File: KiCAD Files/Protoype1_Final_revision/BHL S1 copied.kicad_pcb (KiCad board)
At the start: 4 copper layers, 64 x 64 mm, 104 parts, among them IC1 NUP2105LT1G, IC2 NUP2105LT1G, IC4 FD6288Q, J1 39-30-1042, J2 Conn_01x03_Pin, J3 Conn_01x03_Pin, J4 39-30-1042, Q1 CSD19502Q5B, Q2 CSD19502Q5B, Q3 CSD19502Q5B, Q4 CSD19502Q5B, Q5 CSD19502Q5B, Q7 CSD19502Q5B, U1 ME6211C30M5, U2 SPX3819M5-L-5-0, U3 Solder Pad, U5 STM32G431CBU6, Y1 8MHz

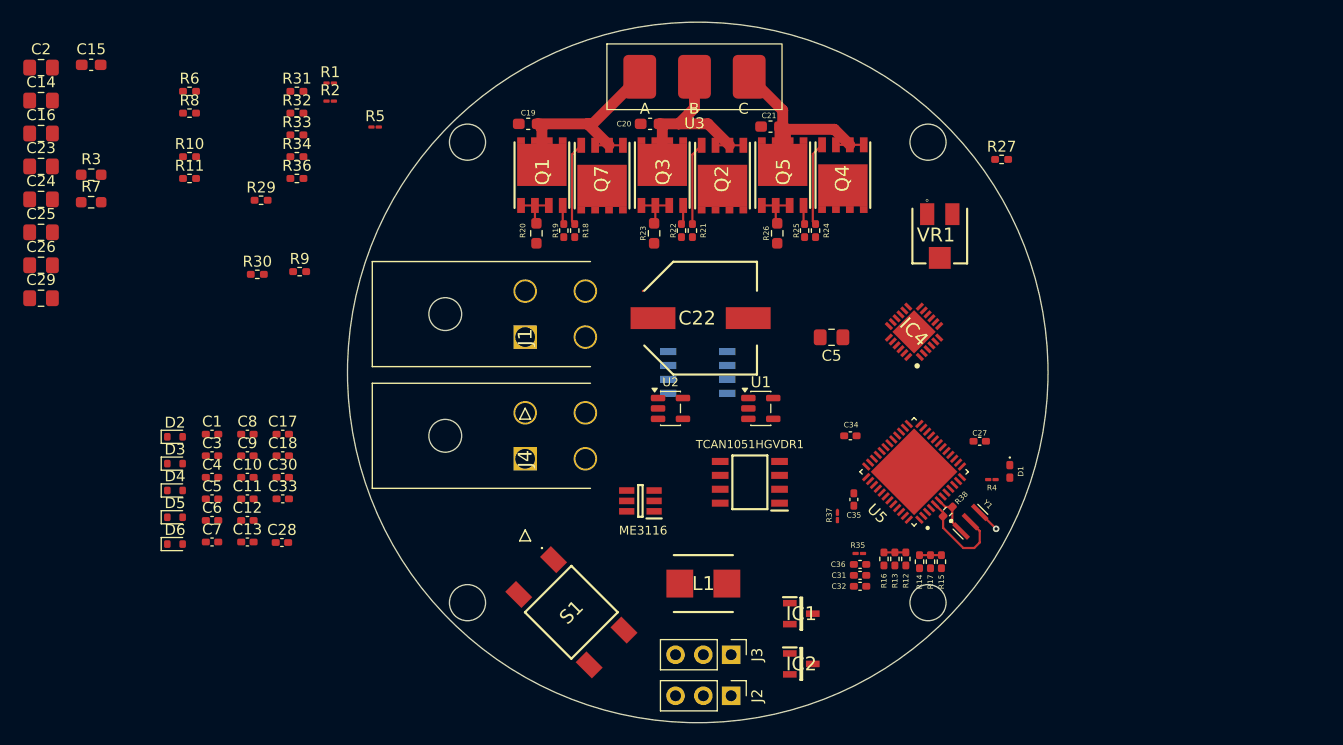
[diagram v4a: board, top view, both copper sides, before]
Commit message: Routed half the gate driver
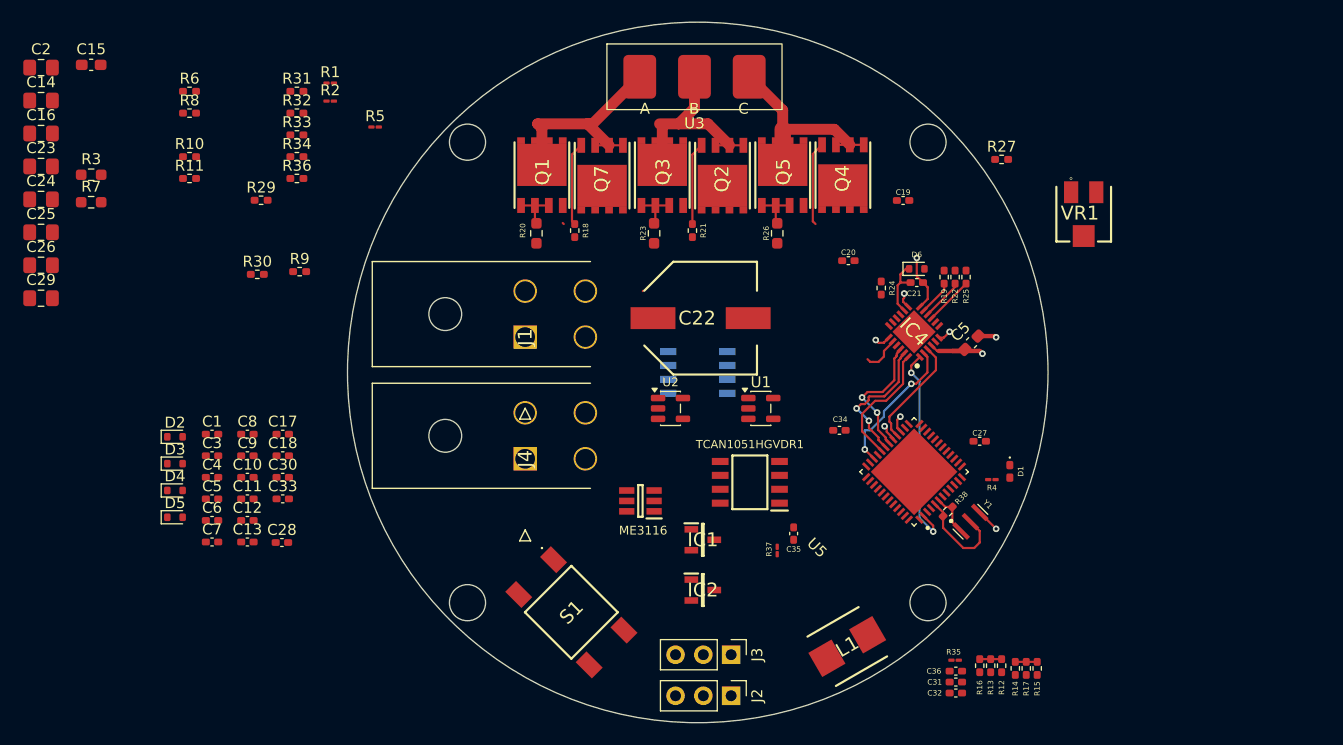
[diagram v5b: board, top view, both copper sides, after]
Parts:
- C19, C20, C21: footprint Capacitor_SMD:C_0603_1608Metric_Pad1.08x0.95mm_HandSolder -> Capacitor_SMD:C_0402_1005Metric_Pad0.74x0.62mm_HandSolder
- C5: footprint Capacitor_SMD:C_0805_2012Metric_Pad1.18x1.45mm_HandSolder -> Capacitor_SMD:C_0603_1608Metric_Pad1.08x0.95mm_HandSolder
- moved D6 72.3 mm to (217.8, 74.0)
- moved R19 35.0 mm to (220.2, 74.8)
- moved C19 35.0 mm to (216.5, 67.8)
- moved R22 25.4 mm to (221.2, 74.8)
- moved C20 22.0 mm to (211.5, 73.2)
- moved C21 19.5 mm to (217.8, 75.2)
- moved R25 15.4 mm to (222.2, 74.8)
- moved L1 14.4 mm to (211.4, 108.5), turned to 30 degrees
- moved VR1 13.3 mm to (233.0, 69.0)
- moved C31 13.1 mm to (221.3, 111.8)
- moved C32 13.1 mm to (221.3, 112.8)
- moved C36 13.1 mm to (221.3, 110.8)
- moved R12 13.1 mm to (225.5, 110.2)
- moved R13 13.1 mm to (223.5, 110.2)
- moved R14 13.1 mm to (226.8, 110.5)
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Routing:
- net LIN1: track 0.00 -> 18.9 mm, vias 0 -> 2
- net LIN2: track 0.00 -> 13.1 mm, vias 0 -> 2
- net HIN2: track 0.00 -> 12.5 mm, vias 0 -> 2
- net HIN1: track 0.00 -> 11.9 mm, vias 0 -> 2
- net HIN3: track 0.00 -> 11.7 mm
- net LIN3: track 0.00 -> 10.3 mm
- net VCC_12V: track 0.00 -> 6.17 mm, vias 0 -> 1
- net VB3: track 0.00 -> 5.60 mm
- net SH_C: track 18.9 -> 24.1 mm, vias 0 -> 1
- net GL_C: track 0.00 -> 4.48 mm
- net GL_B: track 0.00 -> 3.85 mm
- net VB1: track 0.00 -> 3.51 mm
- net GL_A: track 0.00 -> 3.23 mm
- net GND: track 1.77 -> 4.62 mm, vias 1 -> 3
- net Net-(Q3-G): track 1.76 -> 0.00 mm
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
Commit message: Finished Routing the Gate Driver!
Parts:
- R20, R23, R26: footprint Resistor_SMD:R_0603_1608Metric_Pad0.98x0.95mm_HandSolder -> Resistor_SMD:R_1206_3216Metric_Pad1.30x1.75mm_HandSolder
- moved D5 66.6 mm to (213.2, 75.8), turned to 45 degrees
- moved D4 62.4 mm to (210.8, 80.0), turned to 90 degrees
- moved C31 25.4 mm to (246.7, 112.0)
- moved C32 25.4 mm to (246.7, 113.0)
- moved C36 25.4 mm to (246.7, 111.0)
- moved R12 25.4 mm to (250.9, 110.5)
- moved R13 25.4 mm to (248.9, 110.5)
- moved R14 25.4 mm to (252.1, 110.8)
- moved R15 25.4 mm to (254.1, 110.8)
- moved R16 25.4 mm to (249.9, 110.5)
- moved R17 25.4 mm to (253.1, 110.8)
- moved R35 25.4 mm to (246.6, 110.0)
- moved C19 12.8 mm to (212.8, 80.0), turned to 90 degrees
- moved R24 10.4 mm to (204.5, 72.8), turned to 0 degrees
- moved R18 6.77 mm to (179.8, 70.0)
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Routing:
- net GH_A: track 1.51 -> 41.0 mm, vias 1 -> 2
- net Net-(Q1-G): track 0.13 -> 37.3 mm, vias 0 -> 2
- net Net-(Q3-G): track 0.00 -> 27.4 mm, vias 0 -> 2
- net GH_B: track 0.00 -> 24.5 mm, vias 0 -> 2
- net SH_A: track 20.3 -> 40.2 mm, vias 0 -> 2
- net Net-(Q5-G): track 0.00 -> 13.8 mm
- net GH_C: track 1.45 -> 15.2 mm, vias 1 -> 2
- net SH_B: track 18.1 -> 29.4 mm, vias 0 -> 2
- net VB2: track 0.00 -> 5.22 mm
- net SH_C: track 24.1 -> 19.1 mm, vias 1 -> 2
- net VCC_12V: track 6.17 -> 10.6 mm, vias 1 -> 4
- net Vshunt_1+: track 4.33 -> 0.00 mm
- net Vshunt_3+: track 4.23 -> 0.00 mm
- net Vshunt_2+: track 4.22 -> 0.00 mm
- net Net-(Q2-G): track 7.54 -> 11.5 mm
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- added copper zone on In2.Cu, net DCBUS
- added copper zone on F.Cu, net GND
- added copper zone on F.Cu, net SH_A
- added copper zone on F.Cu, net SH_B
- added copper zone on F.Cu, net SH_C
- added copper zone on F.Cu, net Vshunt_1+
- added copper zone on F.Cu, net Vshunt_2+
- added copper zone on F.Cu, net Vshunt_3+

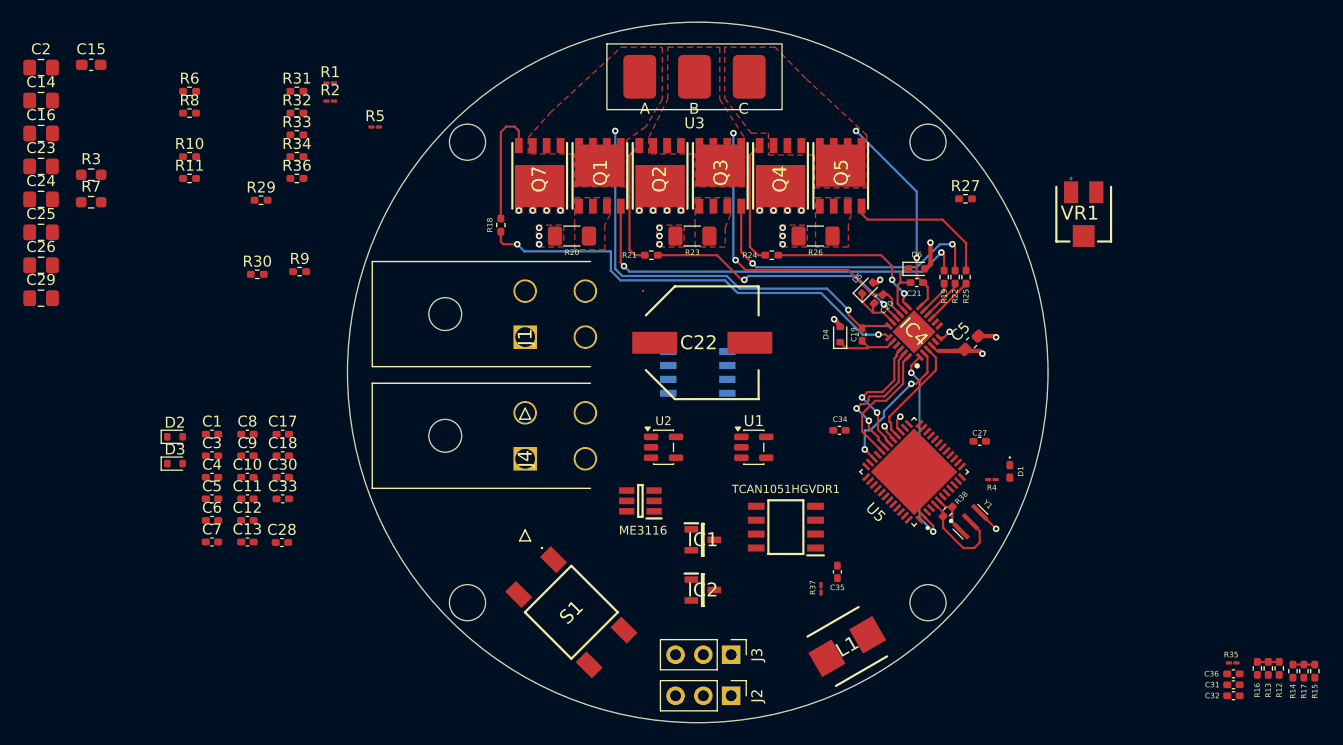
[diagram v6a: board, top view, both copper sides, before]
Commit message: Can Bus Routed In PCB
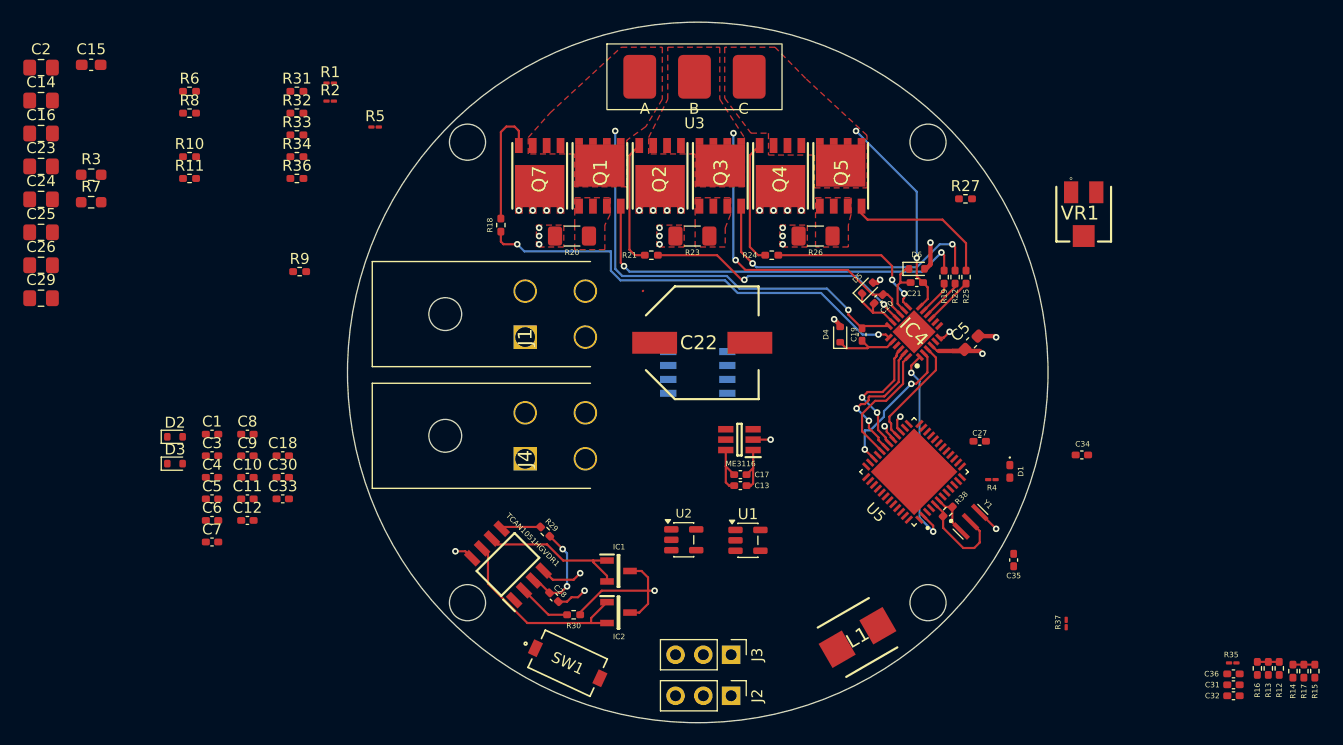
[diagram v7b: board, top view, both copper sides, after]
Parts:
- removed S1: 1571563-6, Footprint for BHL S1:Push Button 6x6mm
- added SW1: PTS636 SM50J SMTR LFS, Footprint for BHL S1:SW_PTS636_CNK, F.Cu at (185.9, 110.0)
- moved C13 45.3 mm to (201.6, 93.8), turned to 180 degrees
- moved R30 42.5 mm to (186.4, 105.6)
- moved C17 42.0 mm to (201.6, 92.8), turned to 180 degrees
- moved R29 39.9 mm to (183.8, 98.0), turned to 135 degrees
- moved TCAN1051HGVDR1 25.6 mm to (180.4, 101.0), turned to 135 degrees
- moved C28 25.3 mm to (184.6, 104.0), turned to -45 degrees
- moved R37 22.6 mm to (231.4, 106.4)
- moved C34 22.3 mm to (232.8, 91.0)
- moved C35 16.1 mm to (226.6, 100.6)
- moved ME3116 10.6 mm to (201.6, 89.6)
- moved U2 8.65 mm to (196.5, 98.8)
- moved U1 8.52 mm to (202.3, 98.8)
- moved IC1 8.21 mm to (190.5, 101.6)
- moved IC2 7.97 mm to (190.5, 105.4)
- moved L1 1.25 mm to (212.3, 107.7)
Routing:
- net GND: track 4.62 -> 29.8 mm, vias 12 -> 16
- net CAN_H: track 0.00 -> 18.3 mm
- net CAN_L: track 0.00 -> 14.0 mm
- net VCC_5V: track 0.00 -> 8.98 mm, vias 0 -> 2
- net Net-(D2-K): track 0.00 -> 4.92 mm
- net Net-(ME3116-BS): track 0.00 -> 4.58 mm
- net CAN_RX: track 0.00 -> 3.93 mm, vias 0 -> 1
- net Net-(TCAN1051HGVDR1-VIO): track 0.00 -> 3.61 mm

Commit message: Finished Buck Converter, Switch, and Temp Resistor Routing
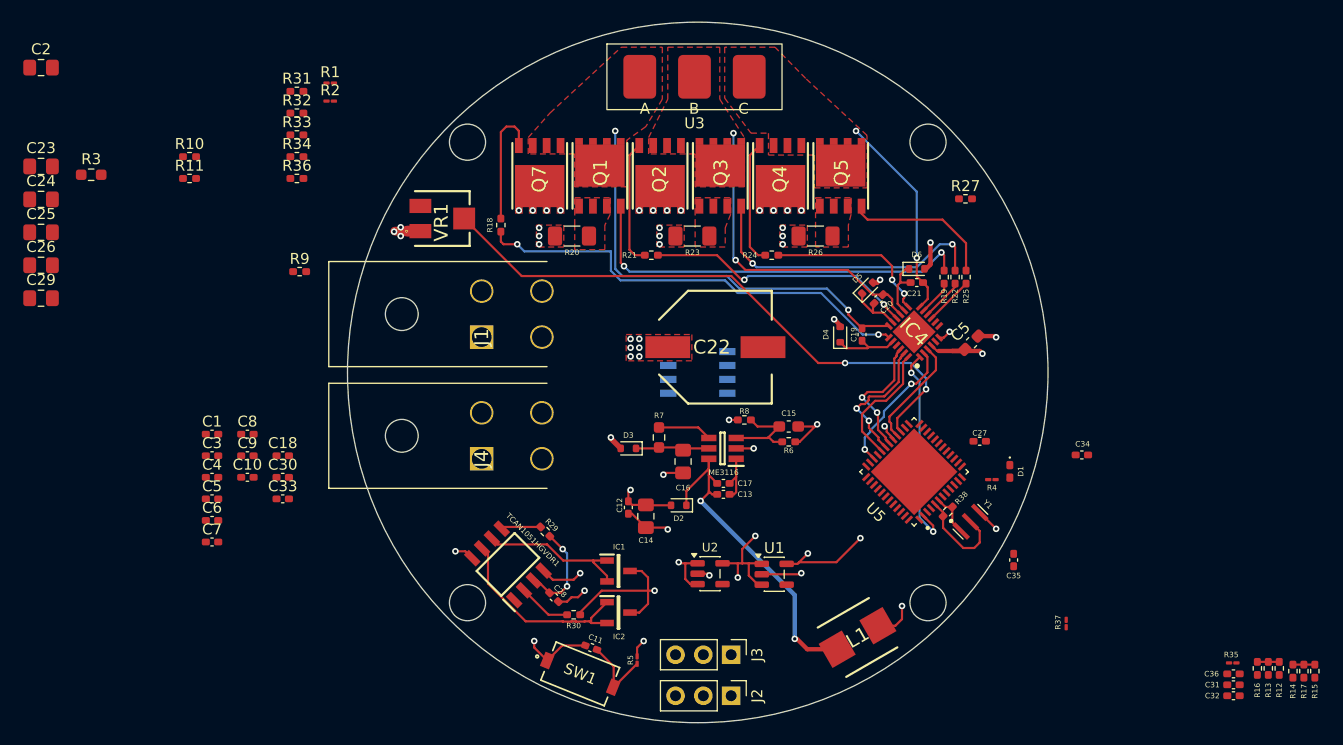
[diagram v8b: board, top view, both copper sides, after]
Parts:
- moved C15 71.8 mm to (206.1, 88.4), turned to 180 degrees
- moved C14 67.1 mm to (193.0, 96.6), turned to 90 degrees
- moved C16 65.9 mm to (196.4, 91.6), turned to 90 degrees
- moved R6 63.4 mm to (206.1, 89.8)
- moved VR1 58.6 mm to (174.4, 69.4), turned to 90 degrees
- moved R8 57.9 mm to (202.0, 87.8)
- moved R7 56.2 mm to (194.2, 89.4), turned to -90 degrees
- moved R5 54.3 mm to (192.2, 109.7), turned to 90 degrees
- moved D2 46.4 mm to (196.0, 95.6), turned to 180 degrees
- moved D3 41.4 mm to (191.4, 90.4), turned to 180 degrees
- moved C12 34.8 mm to (191.4, 95.8), turned to 90 degrees
- moved C11 34.2 mm to (188.0, 108.6), turned to 160 degrees
- moved J1 3.97 mm to (178.0, 80.2)
- moved J4 3.97 mm to (178.0, 91.3)
- moved U1 3.92 mm to (204.7, 101.9)
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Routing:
- net VCC_12V: track 10.6 -> 64.4 mm, vias 4 -> 8
- net TEMP_FEEDBACK: track 1.63 -> 54.4 mm, vias 1 -> 2
- net +3.3V: track 0.00 -> 30.0 mm, vias 0 -> 3
- net Net-(D2-K): track 4.92 -> 31.7 mm, vias 0 -> 2
- net VCC_5V: track 8.98 -> 35.5 mm, vias 2 -> 4
- net GND: track 29.8 -> 48.8 mm, vias 16 -> 22
- net Net-(ME3116-FB): track 0.00 -> 8.62 mm
- net BUTTON: track 0.00 -> 7.15 mm
- net Net-(D3-K): track 0.00 -> 6.86 mm
- net DCBUS: track 0.04 -> 5.17 mm, vias 12 -> 22
- net Net-(ME3116-EN): track 0.00 -> 4.95 mm
- added copper zone on F.Cu, net DCBUS
